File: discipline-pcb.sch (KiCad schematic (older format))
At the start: 169 parts, among them J1 AVR-ISP-6, SW1 KEYSW, SW10 KEYSW, SW11 KEYSW, SW12 KEYSW, SW13 KEYSW, SW14 KEYSW, SW15 KEYSW, SW16 KEYSW, SW17 KEYSW, SW18 KEYSW, SW19 KEYSW, SW2 KEYSW, SW20 KEYSW, SW21 KEYSW, SW22 KEYSW, SW23 KEYSW, SW24 KEYSW, SW25 KEYSW, SW26 KEYSW, SW27 KEYSW, SW28 KEYSW, SW29 KEYSW, SW3 KEYSW, SW30 KEYSW, SW31 KEYSW, SW32 KEYSW, SW33 KEYSW, SW34 KEYSW, SW35 KEYSW, SW36 KEYSW, SW37 KEYSW, SW38 KEYSW, SW39 KEYSW, SW4 KEYSW, SW40 KEYSW, SW41 KEYSW, SW42 KEYSW, SW43 KEYSW, SW44 KEYSW, SW45 KEYSW, SW46 KEYSW, SW47 KEYSW, SW48 KEYSW, SW49 KEYSW, SW5 KEYSW, SW50 KEYSW, SW51 KEYSW, SW52 KEYSW, SW53 KEYSW, SW54 KEYSW, SW55 KEYSW, SW56 KEYSW, SW57 KEYSW, SW58 KEYSW, SW59 KEYSW, SW6 KEYSW, SW60 KEYSW, SW61 KEYSW, SW62 KEYSW, SW63 KEYSW, SW64 KEYSW, SW65 KEYSW, SW66 KEYSW, SW67 KEYSW, SW68 KEYSW, SW69 KEYSW, SW7 KEYSW, SW70 KEYSW, SW71 KEYSW, SW72 KEYSW, SW73 KEYSW, SW74 KEYSW, SW75 KEYSW, SW76 KEYSW, SW77 KEYSW, SW78 KEYSW, SW8 KEYSW, SW9 KEYSW, U1 ATmega32A-PU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

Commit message: modified schematic and footprints for my layout. still need to rearrange traces
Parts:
- removed D68, D71: (no value), cftkb:D_DO-35_SOD27_P5.08mm_Horizontal, symbol Device:D
- removed SW15, SW68, SW72, SW75, SW77: KEYSW, cftkb:SW_Cherry_MX1A_1.00u_PCB-NOSCREEN, symbol keyboard_parts:KEYSW
- removed SW69, SW78: KEYSW, cftkb:SW_Cherry_MX1A_1.25u_PCBNOSCREEN, symbol keyboard_parts:KEYSW
- removed SW70, SW71, SW73, SW74: KEYSW, cftkb:SW_Cherry_MX1A_1.50u_PCBNOSCREEN, symbol keyboard_parts:KEYSW
- removed SW76: KEYSW, cftkb:SW_Cherry_MX1A_ISOEnter_PCB_ReversedStabilizer, symbol keyboard_parts:KEYSW
- added D62, D64: (no value), cftkb:D_DO-35_SOD27_P5.08mm_Horizontal, symbol Device:D
- added SW15: Rotary_Encoder_Switch, Rotary_Encoder:RotaryEncoder_Alps_EC11E-Switch_Vertical_H20mm, symbol Device:Rotary_Encoder_Switch
- added SW62, SW64, SW70: KEYSW-keyboard_parts, cftkb:SW_Cherry_MX1A_2.25u_PCBNOSCREEN, symbol discipline-pcb-rescue:KEYSW-keyboard_parts
- added SW71: KEYSW-keyboard_parts, cftkb:SW_Cherry_MX1A_1.25u_PCBNOSCREEN, symbol discipline-pcb-rescue:KEYSW-keyboard_parts
- added SW72: KEYSW-keyboard_parts, Button_Switch_Keyboard:SW_Cherry_MX_2.75u_PCB, symbol discipline-pcb-rescue:KEYSW-keyboard_parts
- added SW73: KEYSW-keyboard_parts, Button_Switch_Keyboard:SW_Cherry_MX_6.25u_PCB, symbol discipline-pcb-rescue:KEYSW-keyboard_parts
- BOOT1, RESET1: symbol keyboard_parts:SW_PUSH -> discipline-pcb-rescue:SW_PUSH-keyboard_parts
- SW1: footprint cftkb:SW_Cherry_MX1A_1.00u_PCB-NOSCREEN -> Button_Switch_Keyboard:SW_Cherry_MX_1.00u_PCB; symbol keyboard_parts:KEYSW -> discipline-pcb-rescue:KEYSW-keyboard_parts
- SW10, SW11, SW12, SW13, SW14, SW16, SW17, SW18, SW19, SW2, SW20, SW21, SW22, SW23, SW24, SW25, SW26, SW27, SW28, SW29, SW3, SW30, SW31, SW32, SW33, SW34, SW35, SW36, SW37, SW38, SW39, SW4, SW40, SW41, SW42, SW43, SW44, SW45, SW46, SW47, SW48, SW49, SW5, SW50, SW51, SW52, SW53, SW54, SW55, SW56, SW57, SW58, SW59, SW6, SW60, SW61, SW7, SW8, SW9: symbol keyboard_parts:KEYSW -> discipline-pcb-rescue:KEYSW-keyboard_parts
- SW63: renamed from SW62; footprint cftkb:SW_Cherry_MX1A_1.00u_PCB-NOSCREEN -> cftkb:SW_Cherry_MX1A_1.25u_PCBNOSCREEN; symbol keyboard_parts:KEYSW -> discipline-pcb-rescue:KEYSW-keyboard_parts
- SW65: renamed from SW64; footprint cftkb:SW_Cherry_MX1A_1.25u_PCBNOSCREEN -> Button_Switch_Keyboard:SW_Cherry_MX_1.25u_PCB; symbol keyboard_parts:KEYSW -> discipline-pcb-rescue:KEYSW-keyboard_parts
- SW66: renamed from SW63; footprint cftkb:SW_Cherry_MX1A_1.25u_PCBNOSCREEN -> Button_Switch_Keyboard:SW_Cherry_MX_1.25u_PCB; symbol keyboard_parts:KEYSW -> discipline-pcb-rescue:KEYSW-keyboard_parts
- SW67: renamed from SW65; symbol keyboard_parts:KEYSW -> discipline-pcb-rescue:KEYSW-keyboard_parts
- SW68: renamed from SW66; symbol keyboard_parts:KEYSW -> discipline-pcb-rescue:KEYSW-keyboard_parts
- SW69: renamed from SW67; symbol keyboard_parts:KEYSW -> discipline-pcb-rescue:KEYSW-keyboard_parts
- USB1: symbol Type-C:USB_C_GCT_USB4085 -> discipline-pcb-rescue:USB_C_GCT_USB4085-Type-C
- renumbered D62 to D63, D64 to D65, D63 to D66, D65 to D67, D66 to D68, D67 to D69, D69 to D70, D70 to D71
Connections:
- net labels added: encA, encB
- wire segments 353 -> 335
- no-connect marks 9 -> 7
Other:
- moved on the sheet: D66

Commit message: little footprint changes in schematic
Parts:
- SW1: footprint Button_Switch_Keyboard:SW_Cherry_MX_1.00u_PCB -> cftkb:SW_Cherry_MX1A_1.00u_PCB-NOSCREEN
- SW15: footprint Rotary_Encoder:RotaryEncoder_Alps_EC11E-Switch_Vertical_H20mm -> cftkb:RotaryEncoder_Alps_EC11E-Switch_Vertical_H20mm_nosilk
- SW62: footprint cftkb:SW_Cherry_MX1A_2.25u_PCBNOSCREEN -> cftkb:SW_Cherry_MX_2.75u_PCB_nosilk_flippedstabs
- SW64, SW70: footprint cftkb:SW_Cherry_MX1A_2.25u_PCBNOSCREEN -> cftkb:SW_Cherry_MX_2.25u_PCB_nosilk_fliippedstabs
- SW65, SW66: footprint Button_Switch_Keyboard:SW_Cherry_MX_1.25u_PCB -> cftkb:SW_Cherry_MX1A_1.25u_PCBNOSCREEN
- SW72: footprint Button_Switch_Keyboard:SW_Cherry_MX_2.75u_PCB -> cftkb:SW_Cherry_MX_2.75u_PCB_nosilk_flippedstabs
- SW73: footprint Button_Switch_Keyboard:SW_Cherry_MX_6.25u_PCB -> cftkb:SW_Cherry_MX_6.25u_PCB_nosilk_flippedstabs
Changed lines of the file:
@@
 F 0 "SW1" H 3250 3183 60  0000 C CNN
 F 1 "KEYSW" H 3250 2850 60  0001 C CNN
-F 2 "Button_Switch_Keyboard:SW_Cherry_MX_1.00u_PCB" H 3250 2950 60  0001 C CNN
+F 2 "cftkb:SW_Cherry_MX1A_1.00u_PCB-NOSCREEN" H 3250 2950 60  0001 C CNN
 F 3 "" H 3250 2950 60  0000 C CNN
 	1    3250 2950
@@
 F 0 "SW66" H 10950 5483 60  0000 C CNN
 F 1 "KEYSW" H 10950 5150 60  0001 C CNN
-F 2 "Button_Switch_Keyboard:SW_Cherry_MX_1.25u_PCB" H 10950 5250 60  0001 C CNN
+F 2 "cftkb:SW_Cherry_MX1A_1.25u_PCBNOSCREEN" H 10950 5250 60  0001 C CNN
 F 3 "" H 10950 5250 60  0000 C CNN
 	1    10950 5250
@@
 F 0 "SW65" H 10250 5483 60  0000 C CNN
 F 1 "KEYSW" H 10250 5150 60  0001 C CNN
-F 2 "Button_Switch_Keyboard:SW_Cherry_MX_1.25u_PCB" H 10250 5250 60  0001 C CNN
+F 2 "cftkb:SW_Cherry_MX1A_1.25u_PCBNOSCREEN" H 10250 5250 60  0001 C CNN
 F 3 "" H 10250 5250 60  0000 C CNN
 	1    10250 5250
@@
 F 0 "SW62" H 6050 5483 60  0000 C CNN
 F 1 "KEYSW-keyboard_parts" H 6050 5150 60  0001 C CNN
-F 2 "cftkb:SW_Cherry_MX1A_2.25u_PCBNOSCREEN" H 6050 5483 60  0001 C CNN
+F 2 "cftkb:SW_Cherry_MX_2.75u_PCB_nosilk_flippedstabs" H 6050 5483 60  0001 C CNN
 F 3 "" H 6050 5250 60  0000 C CNN
 	1    6050 5250
@@
 F 0 "SW64" H 8850 5483 60  0000 C CNN
 F 1 "KEYSW-keyboard_parts" H 8850 5150 60  0001 C CNN
-F 2 "cftkb:SW_Cherry_MX1A_2.25u_PCBNOSCREEN" H 8850 5483 60  0001 C CNN
+F 2 "cftkb:SW_Cherry_MX_2.25u_PCB_nosilk_fliippedstabs" H 8850 5483 60  0001 C CNN
 F 3 "" H 8850 5250 60  0000 C CNN
 	1    8850 5250
@@
 F 0 "SW70" H 6050 6033 60  0000 C CNN
 F 1 "KEYSW-keyboard_parts" H 6050 5700 60  0001 C CNN
-F 2 "cftkb:SW_Cherry_MX1A_2.25u_PCBNOSCREEN" H 6050 5800 60  0001 C CNN
+F 2 "cftkb:SW_Cherry_MX_2.25u_PCB_nosilk_fliippedstabs" H 6050 5800 60  0001 C CNN
 F 3 "" H 6050 5800 60  0000 C CNN
 	1    6050 5800
@@
 F 0 "SW72" H 8850 6033 60  0000 C CNN
 F 1 "KEYSW-keyboard_parts" H 8850 5700 60  0001 C CNN
-F 2 "Button_Switch_Keyboard:SW_Cherry_MX_2.75u_PCB" H 8850 5800 60  0001 C CNN
+F 2 "cftkb:SW_Cherry_MX_2.75u_PCB_nosilk_flippedstabs" H 8850 5800 60  0001 C CNN
 F 3 "" H 8850 5800 60  0000 C CNN
 	1    8850 5800
@@
 F 0 "SW73" H 7450 6383 60  0000 C CNN
 F 1 "KEYSW-keyboard_parts" H 7450 6050 60  0001 C CNN
-F 2 "Button_Switch_Keyboard:SW_Cherry_MX_6.25u_PCB" H 7450 6150 60  0001 C CNN
+F 2 "cftkb:SW_Cherry_MX_6.25u_PCB_nosilk_flippedstabs" H 7450 6150 60  0001 C CNN
 F 3 "" H 7450 6150 60  0000 C CNN
 	1    7450 6150
@@
 F 0 "SW15" V 12150 2650 50  0000 C CNN
 F 1 "Rotary_Encoder_Switch" H 13000 2926 50  0001 C CNN
-F 2 "Rotary_Encoder:RotaryEncoder_Alps_EC11E-Switch_Vertical_H20mm" H 12850 2810 50  0001 C CNN
+F 2 "cftkb:RotaryEncoder_Alps_EC11E-Switch_Vertical_H20mm_nosilk" H 12850 2810 50  0001 C CNN
 F 3 "~" H 13000 2910 50  0001 C CNN
 	1    13000 2650

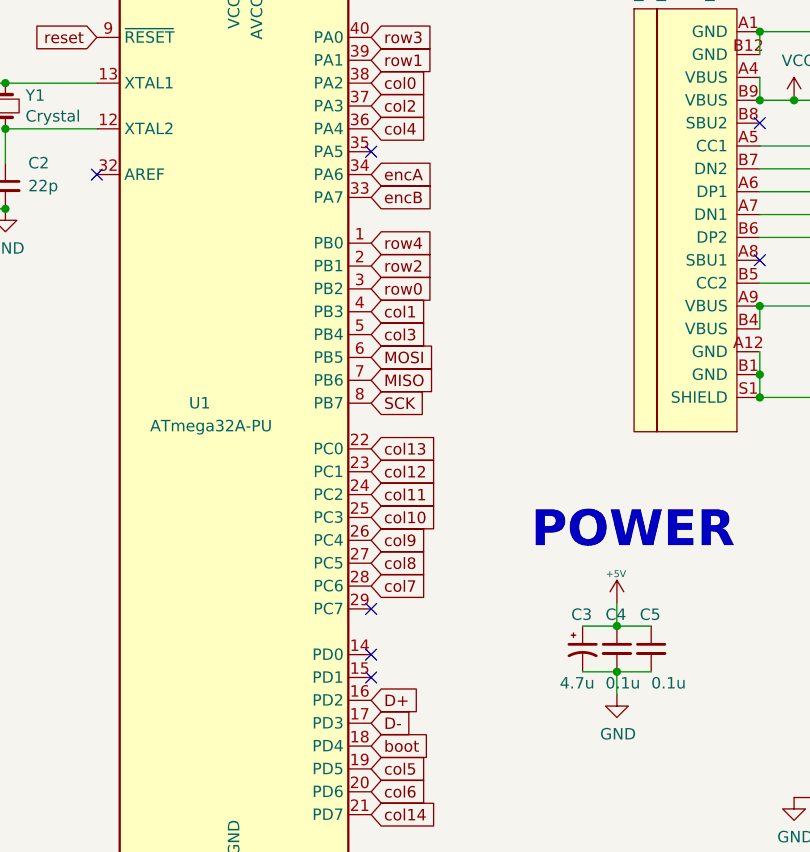
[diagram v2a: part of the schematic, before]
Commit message: traces for matrix columns done
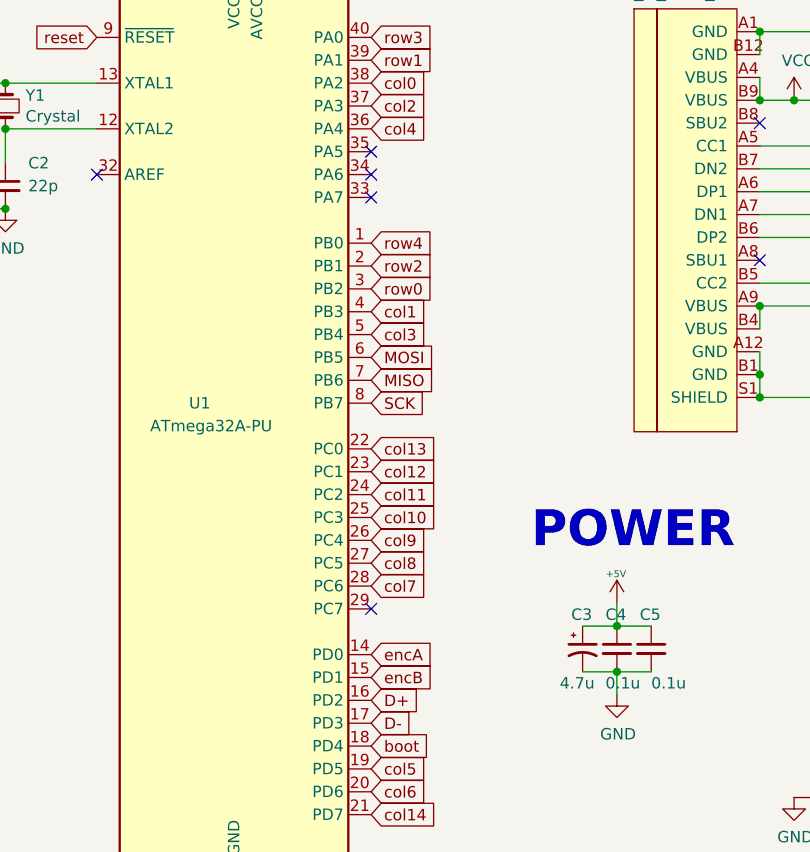
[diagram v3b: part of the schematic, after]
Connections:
- net encA: now also U1.14 (PD0); no longer U1.34 (PA6)
- net encB: now also U1.15 (PD1); no longer U1.33 (PA7)
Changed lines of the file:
@@
 NoConn ~ 4575 7500
 NoConn ~ 4575 9500
-NoConn ~ 4575 9700
-NoConn ~ 4575 9800
 $Comp
 L power:GND #PWR0112
@@
 Wire Wire Line
 	12700 2950 12900 2950
-Text GLabel 4575 7700 2    50   Input ~ 0
+Text GLabel 4575 9800 2    50   Input ~ 0
 encB
-Text GLabel 4575 7600 2    50   Input ~ 0
+Text GLabel 4575 9700 2    50   Input ~ 0
 encA
+NoConn ~ 4575 7600
+NoConn ~ 4575 7700
 $EndSCHEMATC

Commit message: pcb done
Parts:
- SW62, SW64, SW70, SW71, SW72, SW73: value KEYSW-keyboard_parts -> KEYSW
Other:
- note added: "7/18/2021"
- note added: "DISCIPLINE - modded"
- note removed: "1/1/2020"
- note removed: "DISCIPLINE"
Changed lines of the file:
@@
 DISCIPLINE // 65% keyboard with only through hole components
 Text Notes 13000 11050 0    50   ~ 0
-1/1/2020
+7/18/2021
 Text Notes 12250 10900 0    50   ~ 0
-DISCIPLINE
+DISCIPLINE - modded
 Connection ~ 7100 5600
 Connection ~ 9900 5600
@@
 P 6050 5250
 F 0 "SW62" H 6050 5483 60  0000 C CNN
-F 1 "KEYSW-keyboard_parts" H 6050 5150 60  0001 C CNN
+F 1 "KEYSW" H 6050 5150 60  0001 C CNN
 F 2 "cftkb:SW_Cherry_MX_2.75u_PCB_nosilk_flippedstabs" H 6050 5483 60  0001 C CNN
 F 3 "" H 6050 5250 60  0000 C CNN
@@
 P 8850 5250
 F 0 "SW64" H 8850 5483 60  0000 C CNN
-F 1 "KEYSW-keyboard_parts" H 8850 5150 60  0001 C CNN
+F 1 "KEYSW" H 8850 5150 60  0001 C CNN
 F 2 "cftkb:SW_Cherry_MX_2.25u_PCB_nosilk_fliippedstabs" H 8850 5483 60  0001 C CNN
 F 3 "" H 8850 5250 60  0000 C CNN
@@
 P 6050 5800
 F 0 "SW70" H 6050 6033 60  0000 C CNN
-F 1 "KEYSW-keyboard_parts" H 6050 5700 60  0001 C CNN
+F 1 "KEYSW" H 6050 5700 60  0001 C CNN
 F 2 "cftkb:SW_Cherry_MX_2.25u_PCB_nosilk_fliippedstabs" H 6050 5800 60  0001 C CNN
 F 3 "" H 6050 5800 60  0000 C CNN
@@
 P 7450 5800
 F 0 "SW71" H 7450 6033 60  0000 C CNN
-F 1 "KEYSW-keyboard_parts" H 7450 5700 60  0001 C CNN
+F 1 "KEYSW" H 7450 5700 60  0001 C CNN
 F 2 "cftkb:SW_Cherry_MX1A_1.25u_PCBNOSCREEN" H 7450 5800 60  0001 C CNN
 F 3 "" H 7450 5800 60  0000 C CNN
@@
 P 8850 5800
 F 0 "SW72" H 8850 6033 60  0000 C CNN
-F 1 "KEYSW-keyboard_parts" H 8850 5700 60  0001 C CNN
+F 1 "KEYSW" H 8850 5700 60  0001 C CNN
 F 2 "cftkb:SW_Cherry_MX_2.75u_PCB_nosilk_flippedstabs" H 8850 5800 60  0001 C CNN
 F 3 "" H 8850 5800 60  0000 C CNN
@@
 P 7450 6150
 F 0 "SW73" H 7450 6383 60  0000 C CNN
-F 1 "KEYSW-keyboard_parts" H 7450 6050 60  0001 C CNN
+F 1 "KEYSW" H 7450 6050 60  0001 C CNN
 F 2 "cftkb:SW_Cherry_MX_6.25u_PCB_nosilk_flippedstabs" H 7450 6150 60  0001 C CNN
 F 3 "" H 7450 6150 60  0000 C CNN

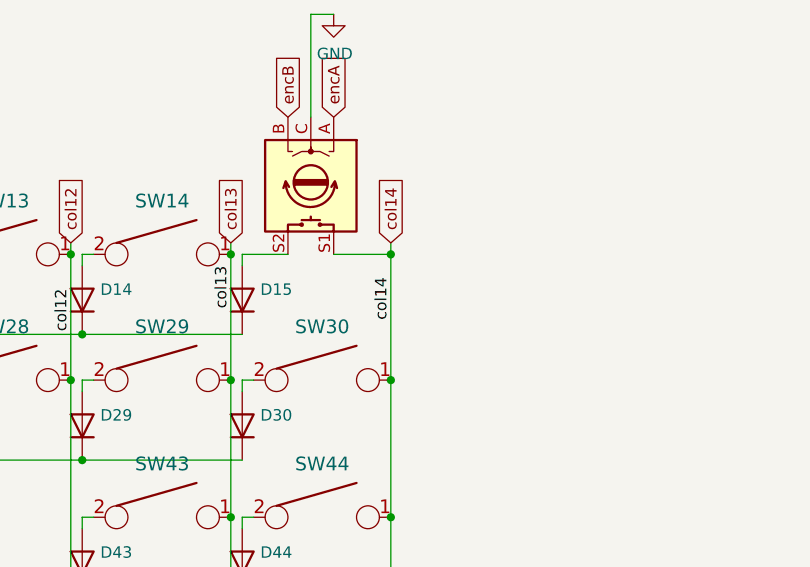
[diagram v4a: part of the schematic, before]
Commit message: turned the rotary encoder slot into a switch/encoder combo slot
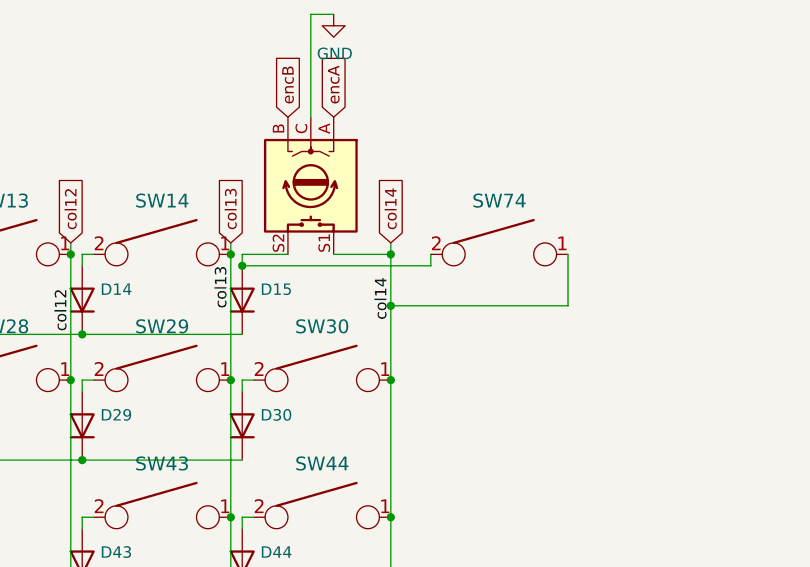
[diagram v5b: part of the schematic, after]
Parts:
- added SW74: KEYSW, cftkb:SW_Cherry_MX1A_1.00u_PCB-NOSCREEN, symbol discipline-pcb-rescue:KEYSW-keyboard_parts
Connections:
- net col14: now also SW74.1
- net at D15.2 (A), SW15.S2: now also SW74.2
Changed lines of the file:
@@
 	12650 2950 12650 3500
 Wire Wire Line
-	13350 2950 13350 3500
+	13350 2950 13350 3175
 Wire Wire Line
 	12700 3300 12000 3300
@@
 NoConn ~ 4575 7600
 NoConn ~ 4575 7700
+$Comp
+L discipline-pcb-rescue:KEYSW-keyboard_parts SW74
+U 1 1 60F8FE34
+P 13825 2950
+F 0 "SW74" H 13825 3183 60  0000 C CNN
+F 1 "KEYSW" H 13825 2850 60  0001 C CNN
+F 2 "cftkb:SW_Cherry_MX1A_1.00u_PCB-NOSCREEN" H 13825 2950 60  0001 C CNN
+F 3 "" H 13825 2950 60  0000 C CNN
+	1    13825 2950
+	1    0    0    -1
+$EndComp
+Wire Wire Line
+	13525 2950 13525 3000
+Wire Wire Line
+	13525 3000 12700 3000
+Connection ~ 12700 3000
+Wire Wire Line
+	14125 2950 14125 3175
+Wire Wire Line
+	14125 3175 13350 3175
+Connection ~ 13350 3175
+Wire Wire Line
+	13350 3175 13350 3500
 $EndSCHEMATC
